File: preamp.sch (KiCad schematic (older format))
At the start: 0 parts

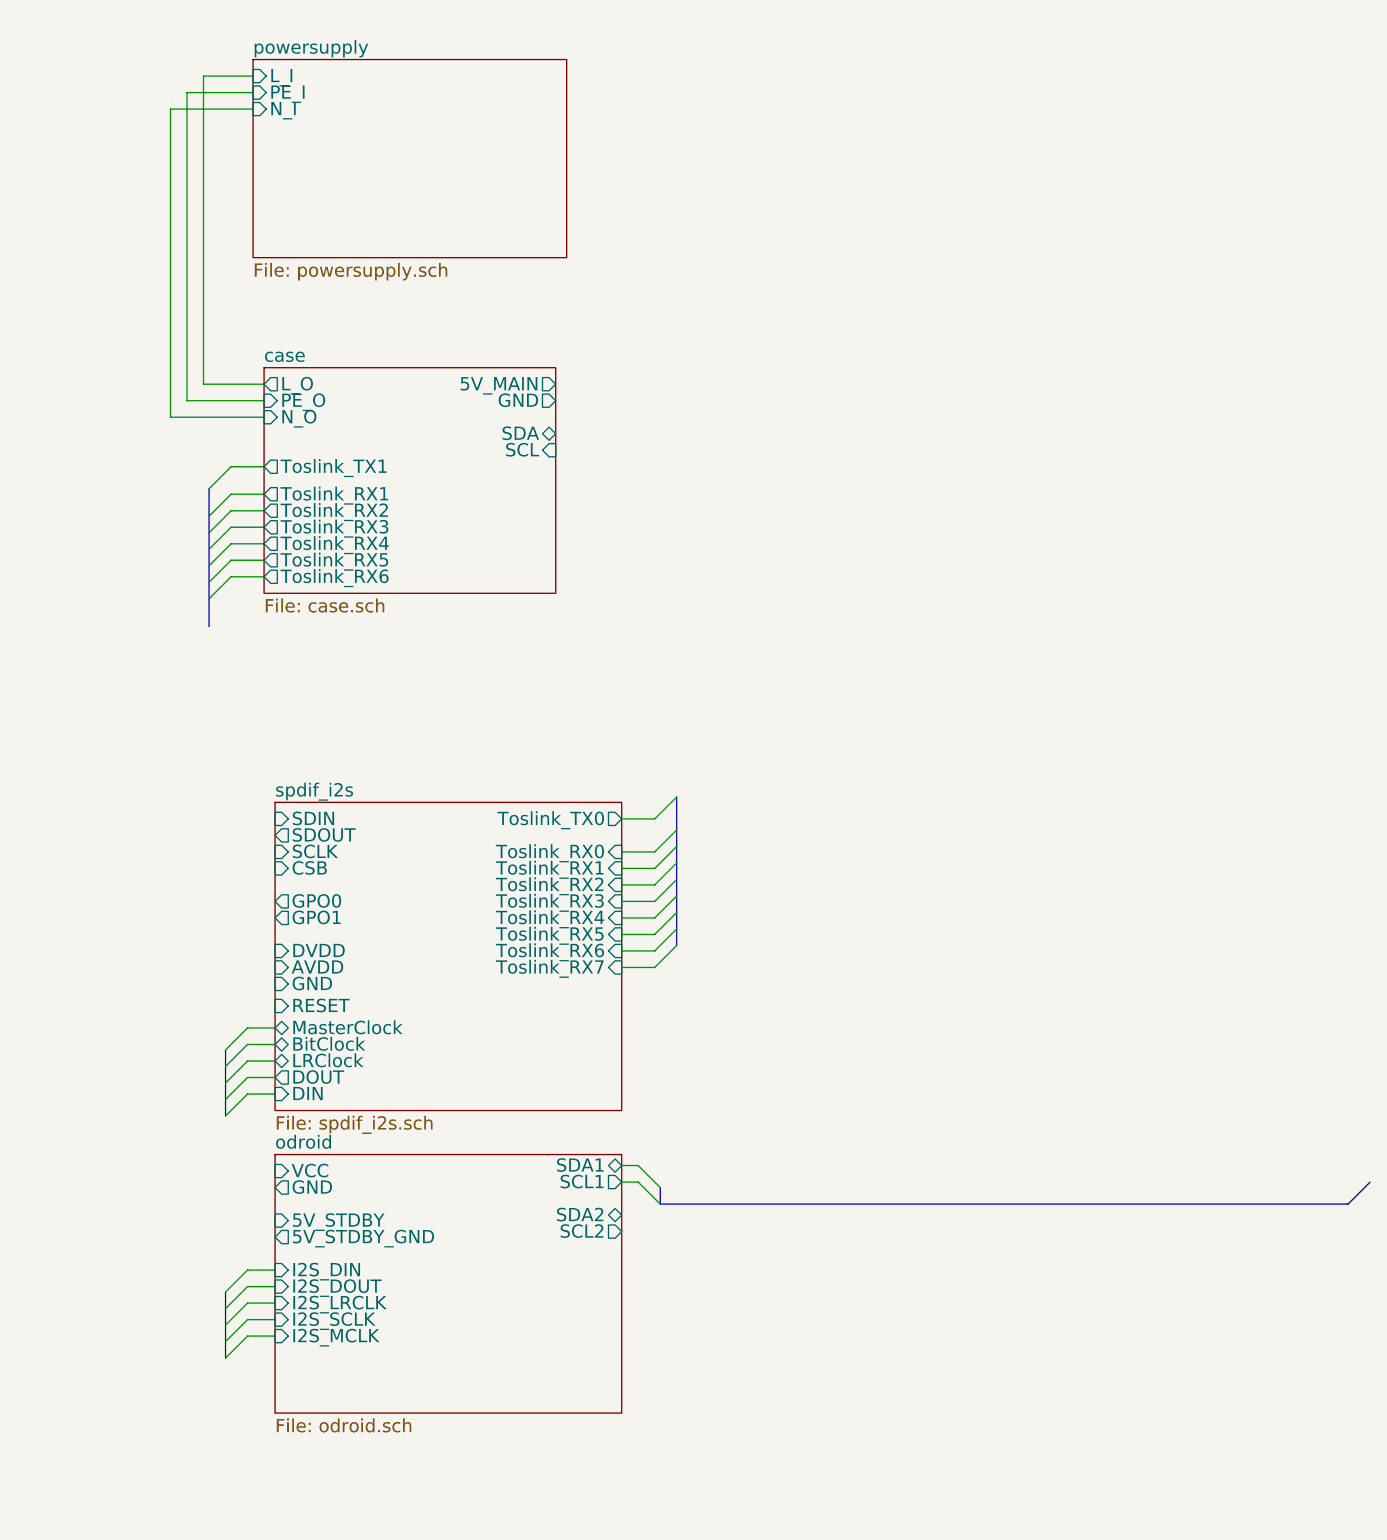
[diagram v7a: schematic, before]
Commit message: phono_preamp and more
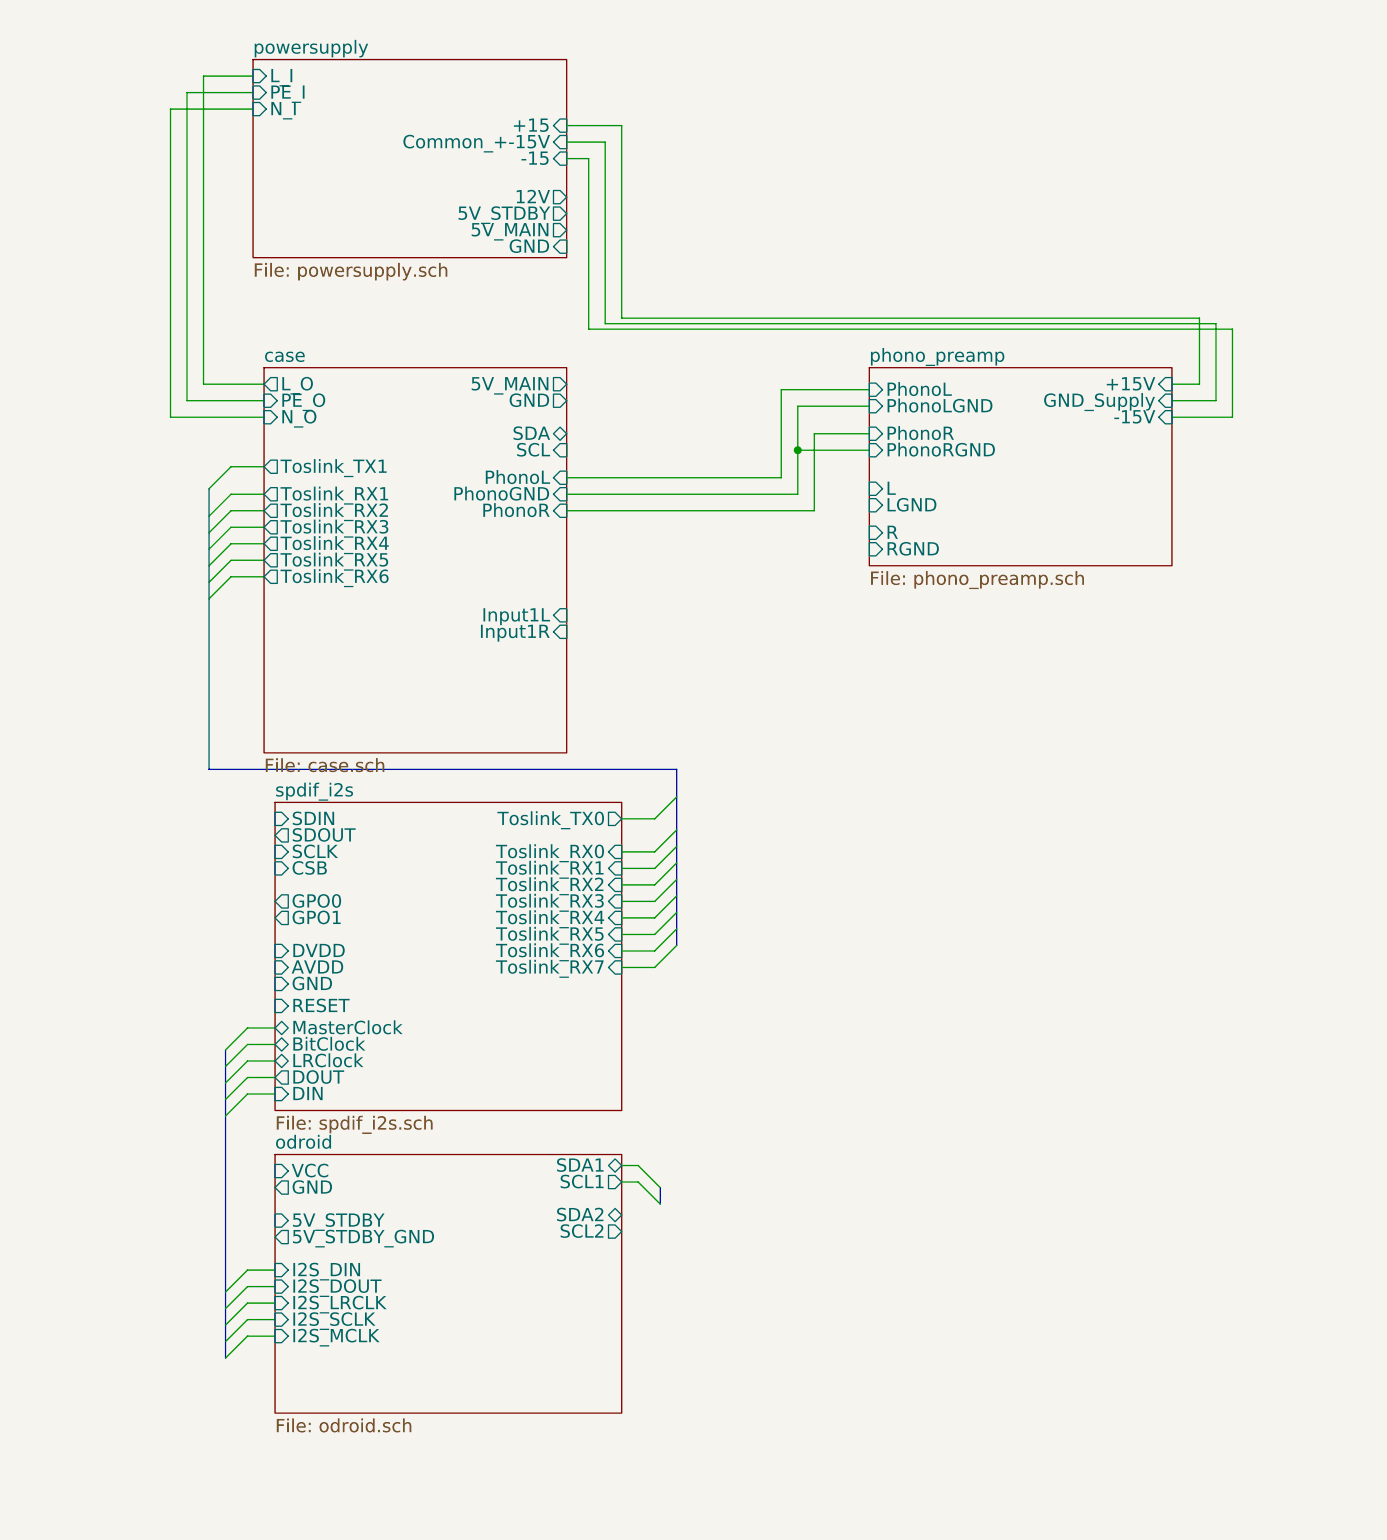
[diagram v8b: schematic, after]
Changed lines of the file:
@@
 $Descr A4 11693 8268
 encoding utf-8
-Sheet 1 13
+Sheet 1 14
 Title ""
 Date ""
@@
 Entry Wire Line
 	3325 6000 3425 6100
-Entry Bus Bus
-	6550 6100 6650 6000
 Wire Wire Line
 	3250 5925 3325 5925
@@
 Wire Bus Line
 	3425 6025 3425 6100
-Wire Bus Line
-	3425 6100 6550 6100
 Entry Wire Line
 	1475 2875 1375 2975
@@
 	1625 3250 1475 3250
 Wire Bus Line
-	1375 2850 1375 3475
-Wire Bus Line
-	3500 4250 3500 4925
+	1375 2850 1375 4125
+Wire Bus Line
+	3500 4125 3500 4925
 Wire Wire Line
 	3250 4500 3400 4500
@@
 	1450 5700 1550 5600
 Wire Bus Line
-	1450 5400 1450 5700
+	1450 5400 1450 6800
 Wire Wire Line
 	1550 5300 1675 5300
@@
 Entry Wire Line
 	1450 6800 1550 6700
-Wire Bus Line
-	1450 6500 1450 6800
 Wire Wire Line
 	1550 6400 1675 6400
@@
 F3 "PE_I" I L 1575 1050 60
 F4 "N_I" I L 1575 1125 60
+F5 "12V" O R 3000 1525 60
+F6 "5V_STDBY" O R 3000 1600 60
+F7 "5V_MAIN" O R 3000 1675 60
+F8 "GND" I R 3000 1750 60
+F9 "Common_+-15V" I R 3000 1275 60
+F10 "+15" I R 3000 1200 60
+F11 "-15" I R 3000 1350 60
 $EndSheet
 Wire Wire Line
@@
 	1200 1125 1575 1125
 $Sheet
-S 1625 2300 1325 1025
+S 1625 2300 1375 1750
 U 5883E969
 F0 "case" 60
 F1 "case.sch" 60
 F2 "PE_O" I L 1625 2450 60
-F3 "GND" O R 2950 2450 60
+F3 "GND" O R 3000 2450 60
 F4 "Toslink_RX1" O L 1625 2875 60
 F5 "Toslink_RX2" O L 1625 2950 60
@@
 F9 "Toslink_RX6" O L 1625 3250 60
 F10 "Toslink_TX1" O L 1625 2750 60
-F11 "SCL" I R 2950 2675 60
-F12 "SDA" B R 2950 2600 60
+F11 "SCL" I R 3000 2675 60
+F12 "SDA" B R 3000 2600 60
 F13 "L_O" O L 1625 2375 60
 F14 "N_O" I L 1625 2525 60
-F15 "5V_MAIN" O R 2950 2375 60
+F15 "5V_MAIN" O R 3000 2375 60
+F16 "PhonoL" I R 3000 2800 60
+F17 "PhonoR" I R 3000 2950 60
+F18 "Input1L" I R 3000 3425 60
+F19 "Input1R" I R 3000 3500 60
+F20 "PhonoGND" I R 3000 2875 60
 $EndSheet
 Entry Wire Line
@@
 Wire Wire Line
 	3400 4350 3250 4350
+Wire Bus Line
+	1375 4125 3500 4125
+$Sheet
+S 4375 2300 1375 900
+U 5939D9BA
+F0 "phono_preamp" 60
+F1 "phono_preamp.sch" 60
+F2 "PhonoL" I L 4375 2400 60
+F3 "PhonoLGND" I L 4375 2475 60
+F4 "PhonoR" I L 4375 2600 60
+F5 "PhonoRGND" I L 4375 2675 60
+F6 "+15V" I R 5750 2375 60
+F7 "-15V" I R 5750 2525 60
+F8 "GND_Supply" I R 5750 2450 60
+F9 "L" I L 4375 2850 60
+F10 "LGND" I L 4375 2925 60
+F11 "R" I L 4375 3050 60
+F12 "RGND" I L 4375 3125 60
+$EndSheet
+Wire Wire Line
+	3000 1350 3100 1350
+Wire Wire Line
+	3100 1350 3100 2125
+Wire Wire Line
+	3100 2125 6025 2125
+Wire Wire Line
+	6025 2125 6025 2525
+Wire Wire Line
+	6025 2525 5750 2525
+Wire Wire Line
+	3000 1275 3175 1275
+Wire Wire Line
+	3175 1275 3175 2100
+Wire Wire Line
+	3175 2100 5950 2100
+Wire Wire Line
+	5950 2100 5950 2450
+Wire Wire Line
+	5950 2450 5750 2450
+Wire Wire Line
+	5750 2375 5875 2375
+Wire Wire Line
+	5875 2375 5875 2075
+Wire Wire Line
+	5875 2075 3250 2075
+Wire Wire Line
+	3250 2075 3250 1200
+Wire Wire Line
+	3250 1200 3000 1200
+Wire Wire Line
+	3000 2800 3975 2800
+Wire Wire Line
+	3975 2800 3975 2400
+Wire Wire Line
+	3975 2400 4375 2400
+Wire Wire Line
+	4375 2475 4050 2475
+Wire Wire Line
+	4050 2475 4050 2875
+Wire Wire Line
+	4050 2875 3000 2875
+Wire Wire Line
+	3000 2950 4125 2950
+Wire Wire Line
+	4125 2950 4125 2600
+Wire Wire Line
+	4125 2600 4375 2600
+Wire Wire Line
+	4375 2675 4050 2675
+Connection ~ 4050 2675
 $EndSCHEMATC
